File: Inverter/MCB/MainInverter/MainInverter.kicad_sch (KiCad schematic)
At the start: 0 parts

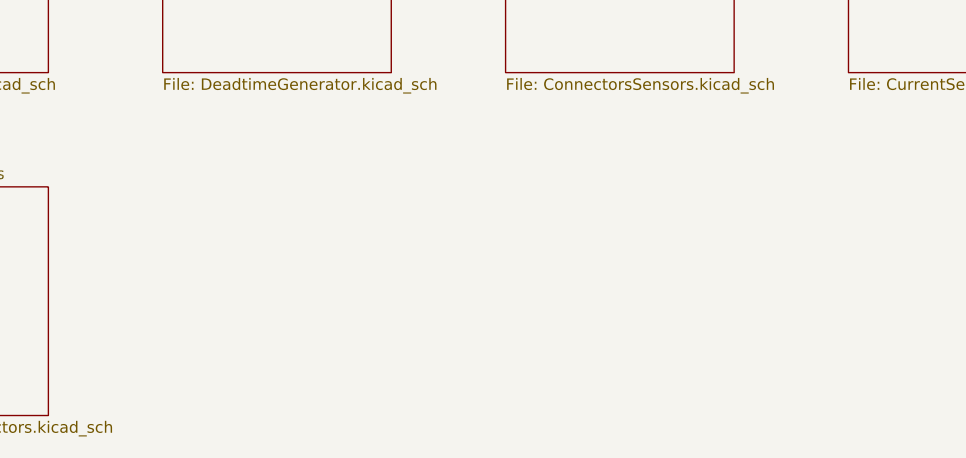
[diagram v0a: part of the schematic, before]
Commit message: Update boost converter, add inverter
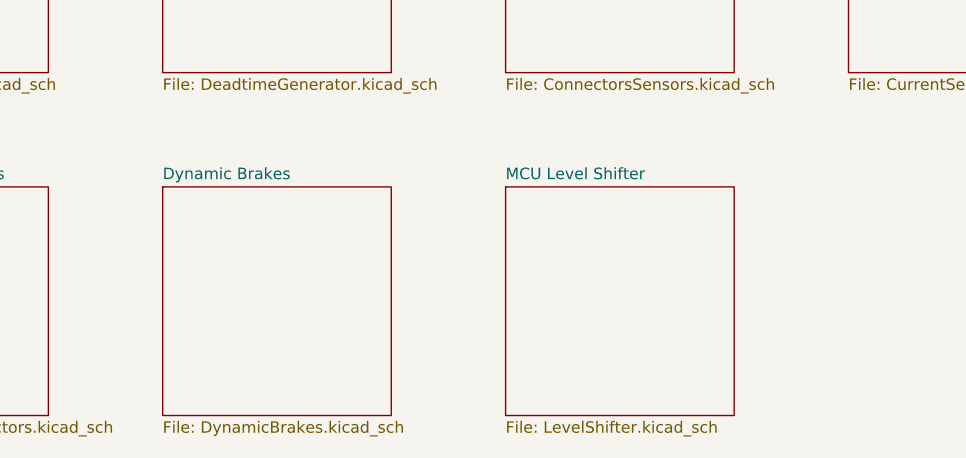
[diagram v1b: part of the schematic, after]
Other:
- added sheet Dynamic Brakes (DynamicBrakes.kicad_sch)
- added sheet MCU Level Shifter (LevelShifter.kicad_sch)
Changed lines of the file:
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@@
+	)
+	(sheet
+		(at 101.6 63.5)
+		(size 25.4 25.4)
+		(fields_autoplaced yes)
+		(stroke
+			(width 0.1524)
+			(type solid)
+		)
+		(fill
+			(color 0 0 0 0.0000)
+		)
+		(property "Sheetname" "MCU Level Shifter"
+			(at 101.6 62.7884 0)
+			(effects
+				(font
+					(size 1.27 1.27)
+				)
+				(justify left bottom)
+			)
+		)
+		(property "Sheetfile" "LevelShifter.kicad_sch"
+			(at 101.6 89.4846 0)
+			(effects
+				(font
+					(size 1.27 1.27)
+				)
+				(justify left top)
+			)
+		)
+		(property "Field2" ""
+			(at 101.6 63.5 0)
+			(effects
+				(font
+					(size 1.27 1.27)
+				)
+				(hide yes)
+			)
+		)
+		(instances
+			(project "MainInverter"
+				(path "/50c926ca-e56d-464e-84a9-9f471dafbf62"
+					(page "11")
+				)
+			)
+		)
 	)
 	(sheet
@@
 				)
 			)
+		)
+	)
+	(sheet
+		(at 63.5 63.5)
+		(size 25.4 25.4)
+		(fields_autoplaced yes)
+		(stroke
+			(width 0.1524)
+			(type solid)
+		)
+		(fill
+			(color 0 0 0 0.0000)
+		)
+		(property "Sheetname" "Dynamic Brakes"
+			(at 63.5 62.7884 0)
+			(effects
+				(font
+					(size 1.27 1.27)
+				)
+				(justify left bottom)
+			)
+		)
+		(property "Sheetfile" "DynamicBrakes.kicad_sch"
+			(at 63.5 89.4846 0)
+			(effects
+				(font
+					(size 1.27 1.27)
+				)
+				(justify left top)
+			)
+		)
+		(instances
+			(project "MainInverter"
+				(path "/50c926ca-e56d-464e-84a9-9f471dafbf62"
+					(page "10")
+				)
+			)
